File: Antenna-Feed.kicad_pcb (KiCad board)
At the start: 2 copper layers, 75 x 97.5 mm, 18 parts, among them J1 Conn_01x01, J10 PC104PTH, J11 PC104PTH, J12 PC104PTH, J13 PC104PTH, J16 Conn_01x03, J17 Conn_01x03, J2 PC104-8BIT, J3 SMA, J4 Conn_01x01, J5 Conn_01x01, J6 Conn_01x01, J7 Conn_01x01, J8 Conn_01x01, SW1 LIMIT_SWITCH, SW2 LIMIT_SWITCH, U1 NC7SZ157, U2 NC7SZ157

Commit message: generated gerbers
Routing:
- added copper zone on B.Cu, net /DEPLOY.+Z
- added copper zone on B.Cu, net /DEPLOY.-Z
- removed copper zone on F.Cu, net /DEPLOY.+Z
- removed copper zone on F.Cu, net /DEPLOY.-Z
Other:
- board text added: "1A"
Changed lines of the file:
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@@
     (links 30)
     (no_connects 0)
-    (area 89.924999 42.464999 162.075001 140.075001)
+    (area 78.58974 40.255 166.245857 144.700001)
     (thickness 1.6)
-    (drawings 10)
+    (drawings 12)
     (tracks 100)
     (zones 0)
@@
     (user_trace_width 3.5)
     (trace_clearance 0.1524)
-    (zone_clearance 0.254)
+    (zone_clearance 0.1524)
     (zone_45_only no)
     (trace_min 0.1524)
@@
     (visible_elements FFFFFF7F)
     (pcbplotparams
-      (layerselection 0x00030_80000001)
+      (layerselection 0x010f0_80000001)
       (usegerberextensions false)
       (excludeedgelayer true)
@@
       (psa4output false)
       (plotreference true)
-      (plotvalue true)
+      (plotvalue false)
       (plotinvisibletext false)
       (padsonsilk false)
@@
       (outputformat 1)
       (mirror false)
-      (drillshape 1)
+      (drillshape 0)
       (scaleselection 1)
-      (outputdirectory ""))
+      (outputdirectory Fab/))
   )
   (net 0 "")
@@
     )
   )
+  (gr_text 1A (at 162.75 135.25) (layer B.Mask)
+    (effects (font (size 1 1) (thickness 0.15)) (justify mirror))
+  )
+  (gr_text 1A (at 162.75 135.25) (layer F.SilkS)
+    (effects (font (size 1 1) (thickness 0.15)))
+  )
   (gr_line (start 90 140) (end 90 42.54) (layer Edge.Cuts) (width 0.15))
   (gr_line (start 165 140) (end 165 42.54) (layer Edge.Cuts) (width 0.15))
@@
     )
   )
-  (zone (net 47) (net_name /DEPLOY.-Z) (layer F.Cu) (hatch edge 0.508)
+  (zone (net 48) (net_name /DEPLOY.+Z) (layer B.Cu) (hatch edge 0.508)
+    (priority 1)
+    (connect_pads yes (clearance 0.2))
+    (min_thickness 0.254)
+    (fill yes (arc_segments 16) (thermal_gap 0.508) (thermal_bridge_width 0.508))
+    (polygon
+      (pts
+        (xy 164.991406 70.25) (xy 164.991406 78.5) (xy 151.491406 78.5) (xy 151.491406 72.5) (xy 153.741406 72.5)
+        (xy 154.241406 72) (xy 154.241406 70.25)
+      )
+    )
+  )
+  (zone (net 47) (net_name /DEPLOY.-Z) (layer B.Cu) (hatch edge 0.508)
     (connect_pads yes (clearance 0.1524))
     (min_thickness 0.254)
@@
       )
     )
-  )
-  (zone (net 48) (net_name /DEPLOY.+Z) (layer F.Cu) (hatch edge 0.508)
-    (priority 1)
-    (connect_pads yes (clearance 0.2))
-    (min_thickness 0.254)
-    (fill yes (arc_segments 16) (thermal_gap 0.508) (thermal_bridge_width 0.508))
-    (polygon
-      (pts
-        (xy 165 70.25) (xy 165 78.5) (xy 151.5 78.5) (xy 151.5 72.5) (xy 153.75 72.5)
-        (xy 154.25 72) (xy 154.25 70.25)
-      )
-    )

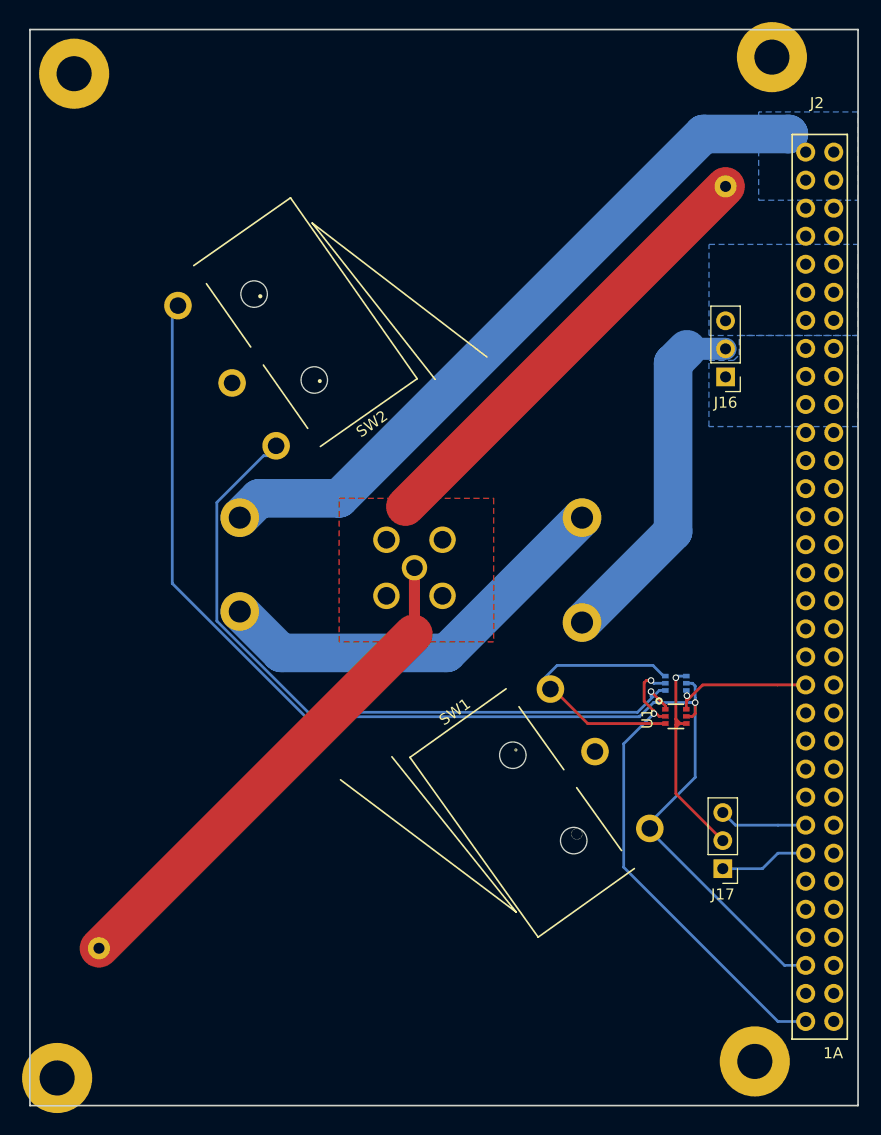
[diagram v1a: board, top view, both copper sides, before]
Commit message: added deployment connections
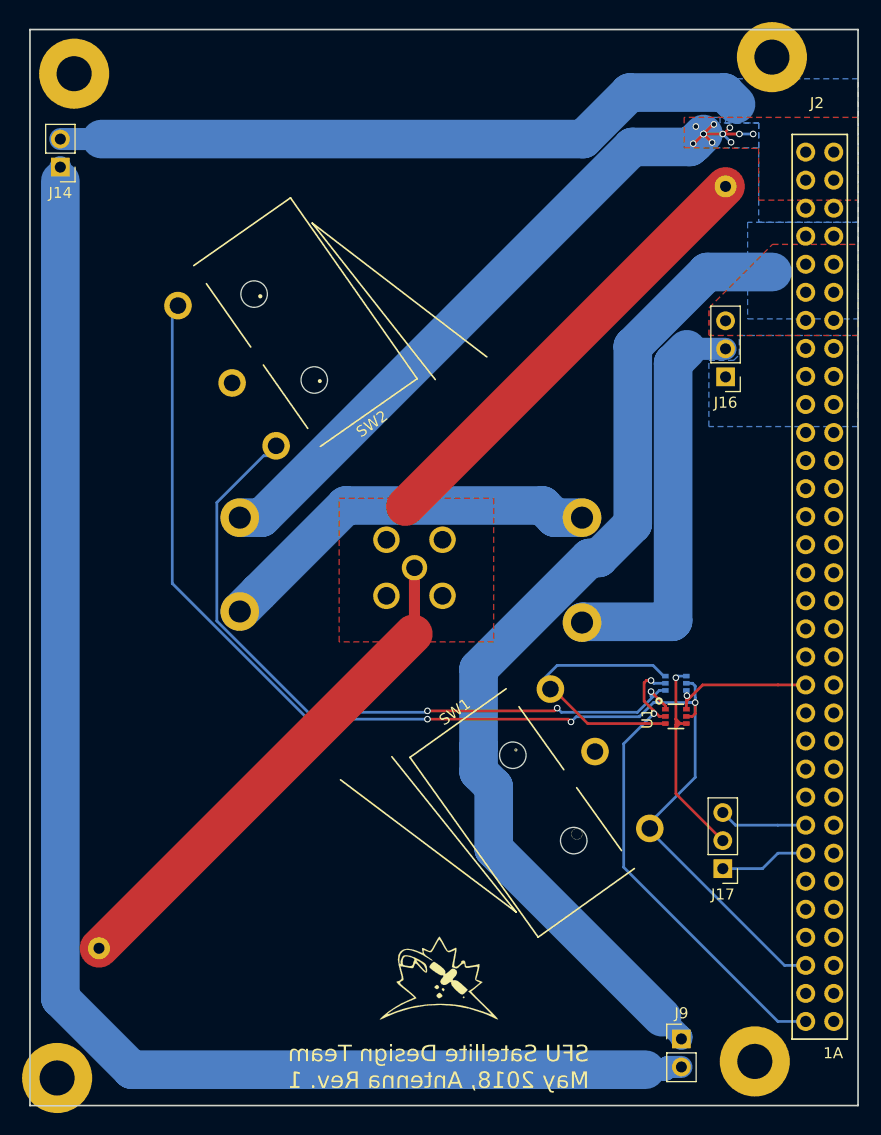
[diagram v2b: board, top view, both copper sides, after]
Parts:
- added G***: LOGO, SFUSat:SFUSat_15mm_2, F.Cu at (127.0, 128.5)
- added J14: Conn_01x02, Socket_Strips:Socket_Strip_Straight_1x02_Pitch2.54mm, F.Cu at (92.8, 55.0)
- added J9: Conn_01x02, Socket_Strips:Socket_Strip_Straight_1x02_Pitch2.54mm, F.Cu at (149.0, 134.0)
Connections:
- J2 pad 28A: Net-(J2-Pad28A) -> /VSYS_DOWN
- J2 pad 29A: Net-(J2-Pad29A) -> /VSYS_DOWN
- J2 pad 30A: Net-(J2-Pad30A) -> /VSYS_UP
- J2 pad 31A: Net-(J2-Pad31A) -> /VSYS_UP
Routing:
- net Net-(J14-Pad1): track 0.00 -> 134.3 mm
- net /VSYS_DOWN: track 0.00 -> 92.0 mm
- net /VSYS_UP: track 0.00 -> 63.4 mm
- net /GNDPWR: track 64.1 -> 69.2 mm, vias 0 -> 11
- net Net-(J16-Pad2): track 34.0 -> 38.7 mm
- net Net-(J6-Pad1): track 37.6 -> 35.4 mm
- net /3V3: track 115.1 -> 115.5 mm, vias 1 -> 3
- net /MUX/IN1: track 66.1 -> 66.4 mm, vias 1 -> 3
- added copper zone on F.Cu, net /DEPLOY.-Z
- added copper zone on F.Cu, net /GNDPWR
- added copper zone on B.Cu, net /VSYS_DOWN
- added copper zone on B.Cu, net /VSYS_UP
- removed copper zone on B.Cu, net /DEPLOY.-Z
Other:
- board text added: "SFU Satellite Design Team May 2018, Antenna Rev. 1"
- board text added: "X+"
- board text added: "X-"
- board text added: "Y-"
- board text added: "y+"

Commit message: board rev 2 complete
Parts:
- removed J10, J11, J12, J13: PC104PTH, SFUSat:PC104PTH
- added J15: Conn_01x01, SFUSat:PTH-2.5, F.Cu at (97.4, 92.1)
- added J18: Conn_01x01, SFUSat:PTH-2.5, F.Cu at (152.3, 90.4)
- added REF**: NPTH-1.75mm, SFUSat:NPTH-1.75mm, F.Cu at (92.5, 137.5)
- added REF**: NPTH-3mm, SFUSat:NPTH-3mm, F.Cu at (152.3, 80.5)
- added REF**: NPTH-3mm, SFUSat:NPTH-3mm, F.Cu at (156.7, 135.0)
- added REF**: NPTH-3mm, SFUSat:NPTH-3mm, F.Cu at (97.4, 102.1)
- added REF**: NPTH-3mm, SFUSat:NPTH-3mm, F.Cu at (93.0, 45.5)
- added REF**: NPTH-1.75mm, SFUSat:NPTH-1.75mm, F.Cu at (157.2, 45.1)
- J5, J6, J7, J8: footprint SFUSat:PTH-2.0mm -> SFUSat:PTH-2.5
- moved J6 7.43 mm to (116.4, 95.9)
- moved J5 7.40 mm to (116.4, 86.8)
- moved J8 6.72 mm to (133.3, 95.8)
- moved J7 6.70 mm to (133.3, 86.8)
- moved J17 3.00 mm to (149.8, 118.5)
- moved J2 2.14 mm to (161.5, 90.9)
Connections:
- J7 pad 1: Net-(J6-Pad1) -> Net-(J16-Pad2)
- J8 pad 1: Net-(J16-Pad2) -> Net-(J6-Pad1)
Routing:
- net /VSYS_DOWN: track 92.0 -> 69.8 mm
- net Net-(J16-Pad2): track 38.7 -> 26.1 mm
- net Net-(J6-Pad1): track 35.4 -> 25.4 mm
- net /GNDPWR: track 69.2 -> 64.9 mm, vias 11 -> 9
- net /RF.DEPLOY0: track 8.09 -> 12.0 mm
- net /RF.DEPLOY1: track 7.98 -> 10.9 mm
- net /3V3: track 115.5 -> 116.8 mm
- net /MUX/OUT: track 19.6 -> 18.4 mm
- net /RF.DEPLOY2: track 13.2 -> 14.0 mm
- net GND: track 43.8 -> 43.4 mm, vias 2 -> 3
- added copper zone on F.Cu, net /DEPLOY.+Z
- removed copper zone on B.Cu, net /DEPLOY.+Z
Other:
- board size 75 x 97.5 mm -> 74 x 97.5 mm
- board text added: "3V3"
- board text added: "DPL0"
- board text added: "DPL1"
- board text added: "DPL2"
- board text added: "GND"
- board text added: "SFU Satellite Design Team May 2018, Antenna Rev. 2"
- board text added: "z+"
- board text added: "z-"
- board text removed: "SFU Satellite Design Team May 2018, Antenna Rev. 1"
